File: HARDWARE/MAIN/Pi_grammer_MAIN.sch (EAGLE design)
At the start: 57 parts, among them J3 RA 6Pin SMD, Q1 220mA/50V/3.5Ω, Q2 220mA/50V/3.5Ω, Q3 220mA/50V/3.5Ω, Q4 220mA/50V/3.5Ω, Q5 220mA/50V/3.5Ω, U1 AT42QT1010 - UDFN, U2 74LVC4066

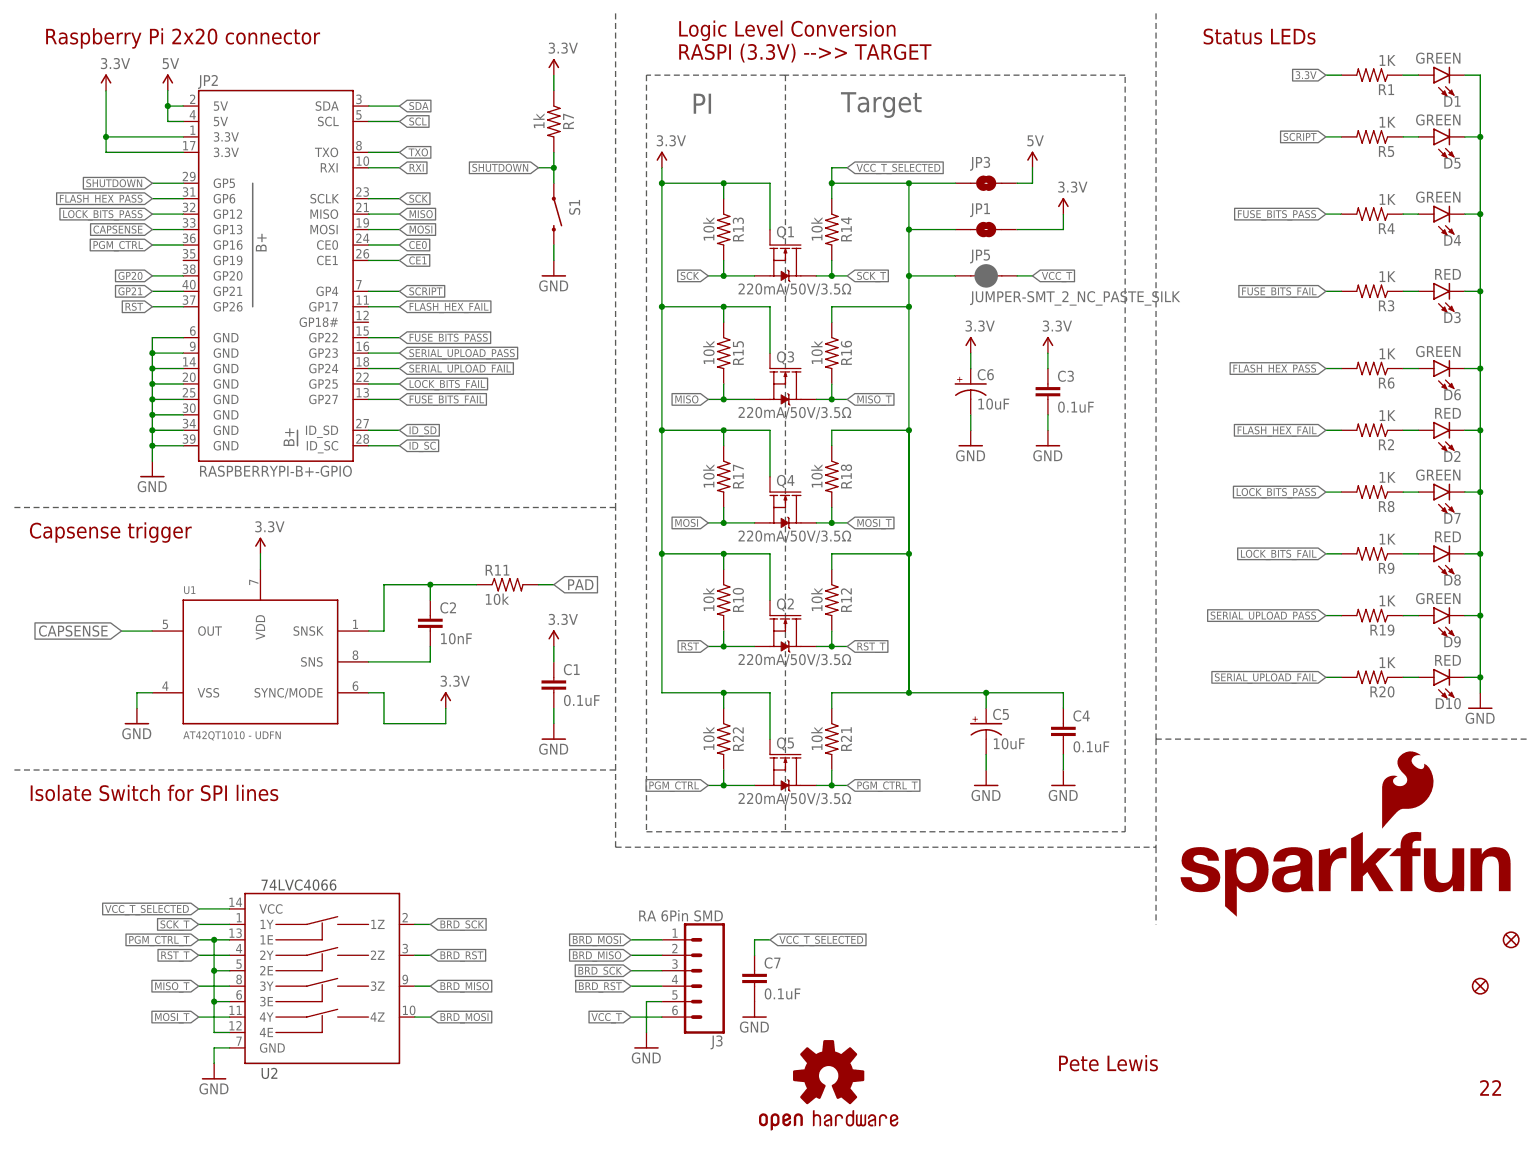
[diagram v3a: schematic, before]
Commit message: schematic frame update to CC 4.0
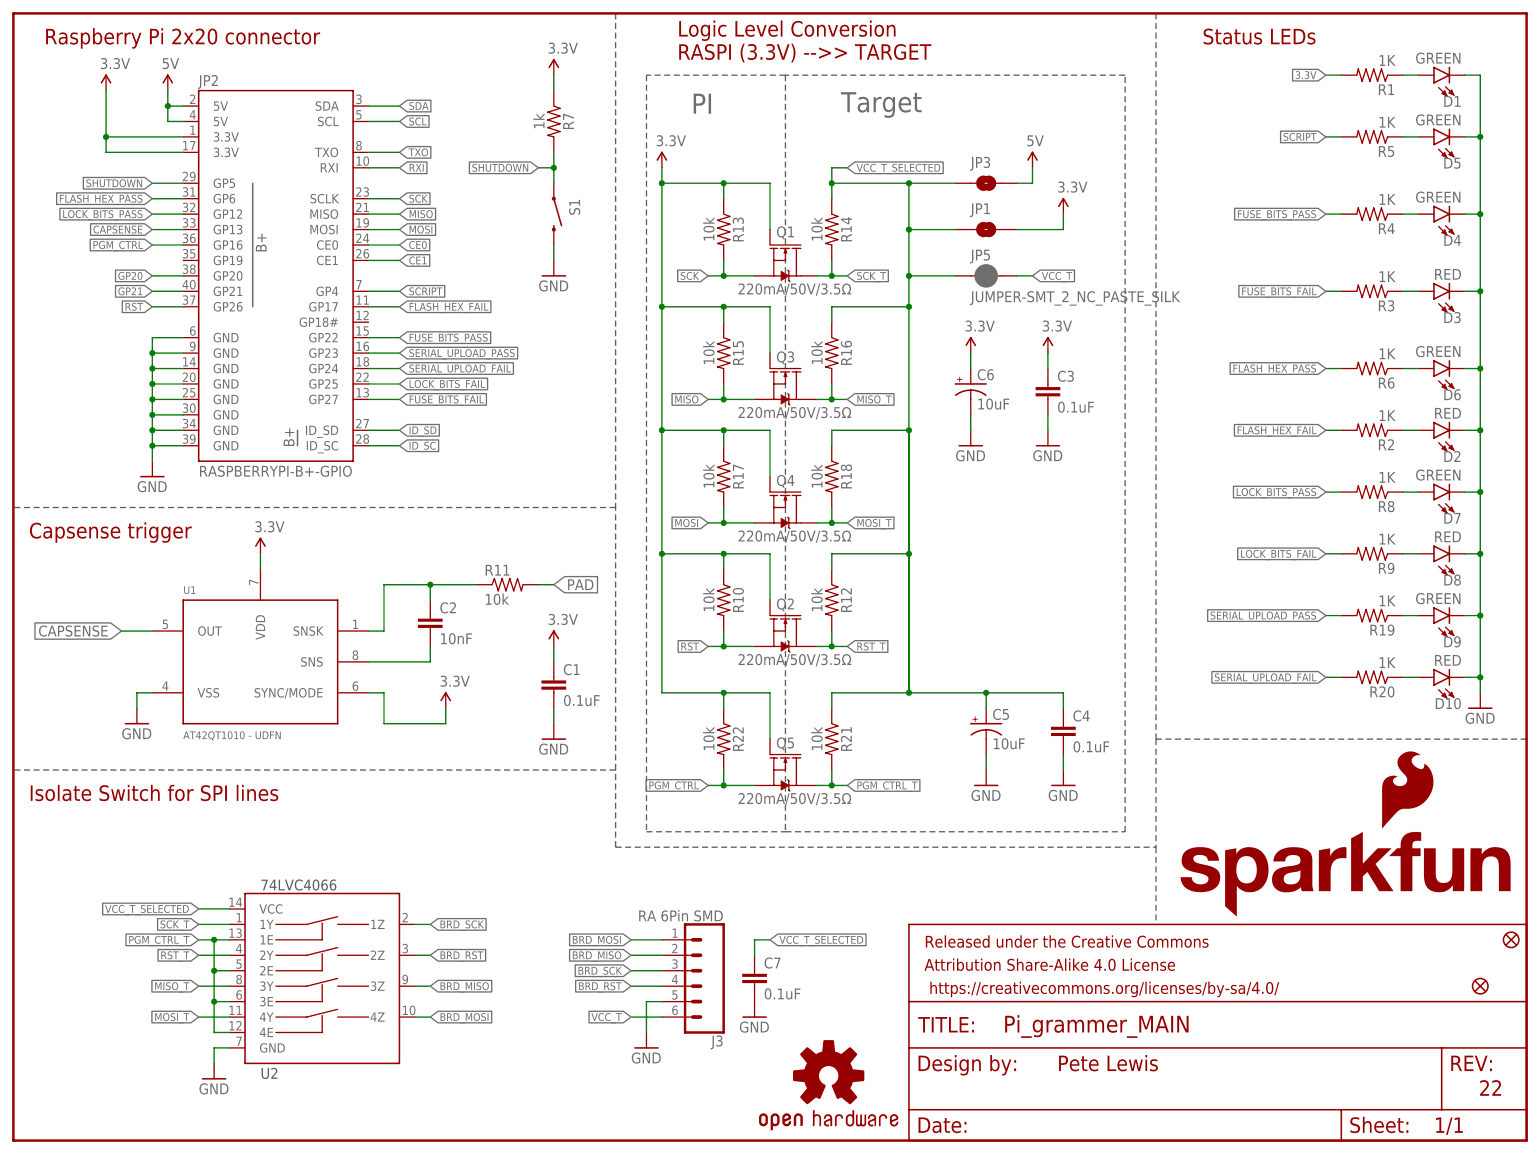
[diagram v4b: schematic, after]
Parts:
- added FRAME1: FRAME-LETTER, SparkFun-Aesthetics:FRAME-LETTER
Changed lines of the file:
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@@
 <instance part="R9" gate="G$1" x="231.14" y="279.4" rot="R180"/>
 <instance part="FRAME1" gate="G$1" x="7.62" y="182.88"/>
-<instance part="FRAME1" gate="G$2" x="154.94" y="182.88"/>
+<instance part="FRAME1" gate="V" x="154.94" y="182.88"/>
 <instance part="FD1" gate="G$1" x="248.92" y="208.28"/>
 <instance part="FD2" gate="G$1" x="254" y="215.9"/>

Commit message: schematic cleanup and notes
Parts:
- added FD3, FD4: FIDUCIALUFIDUCIAL, SparkFun-Aesthetics:FIDUCIALUFIDUCIAL
- J2: value RA 6Pin SMD -> SPI
- renumbered J3 to J2, JP2 to J1
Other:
- note added: "Close one of these jumpers to select target logic level. Default is "target" which means the target supplies the logic level for the conversion."
- moved on the sheet: C3, C6, D1, D3, D4, D5, R1, R3, R4, R5

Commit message: prod_ID correction on at42QT1010
manually adjusted from the old package part in sparkle to the new UDFN
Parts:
- J1: PROD_ID (none) -> CONN-13502
- U1: PROD_ID IC-11778 -> (none)
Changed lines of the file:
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@@
 </classes>
 <parts>
-<part name="J1" library="SparkFun-Boards" deviceset="RASPBERRYPI-B+-GPIO" device=""/>
+<part name="J1" library="SparkFun-Boards" deviceset="RASPBERRYPI-B+-GPIO" device="">
+<attribute name="PROD_ID" value="CONN-13502"/>
+</part>
 <part name="GND9" library="SparkFun" deviceset="GND" device=""/>
 <part name="SUPPLY13" library="SparkFun-Aesthetics" deviceset="5V" device=""/>
@@
 <part name="D7" library="SparkFun-LED" deviceset="LED-GREEN" device="1206" value="GREEN"/>
 <part name="LOGO2" library="SparkFun-Aesthetics" deviceset="OSHW-LOGO" device="L" value="OSHW-LOGOL"/>
-<part name="U1" library="SparkFun-Sensors" deviceset="AT42QT1010" device="UDFN" value="AT42QT1010 - UDFN">
-<attribute name="PROD_ID" value="IC-11778"/>
-</part>
+<part name="U1" library="SparkFun-Sensors" deviceset="AT42QT1010" device="UDFN" value="AT42QT1010 - UDFN"/>
 <part name="C1" library="SparkFun-Capacitors" deviceset="0.1UF-25V(+80/-20%)(0603)" device="" value="0.1uF"/>
 <part name="C2" library="SparkFun-Capacitors" deviceset="10NF/10000PF-50V-10%(0603)" device="" value="10nF"/>
@@
 </plain>
 <instances>
-<instance part="J1" gate="G$1" x="50.8" y="327.66"/>
+<instance part="J1" gate="G$1" x="50.8" y="327.66">
+<attribute name="PROD_ID" x="50.8" y="327.66" size="1.27" layer="96" font="vector" display="off"/>
+</instance>
 <instance part="GND9" gate="1" x="30.48" y="292.1"/>
 <instance part="SUPPLY13" gate="G$1" x="33.02" y="355.6"/>
